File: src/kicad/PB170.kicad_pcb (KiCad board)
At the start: 4 copper layers, 61 parts, among them J2 USB_B_Micro, Q1 BC817, Q2 BC817, Q3 BC817, Q4 BC817, SW1 SW_MEC_5E, U1 74HC08, U10 74HC08, U2 74HC08, U21 74HC08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

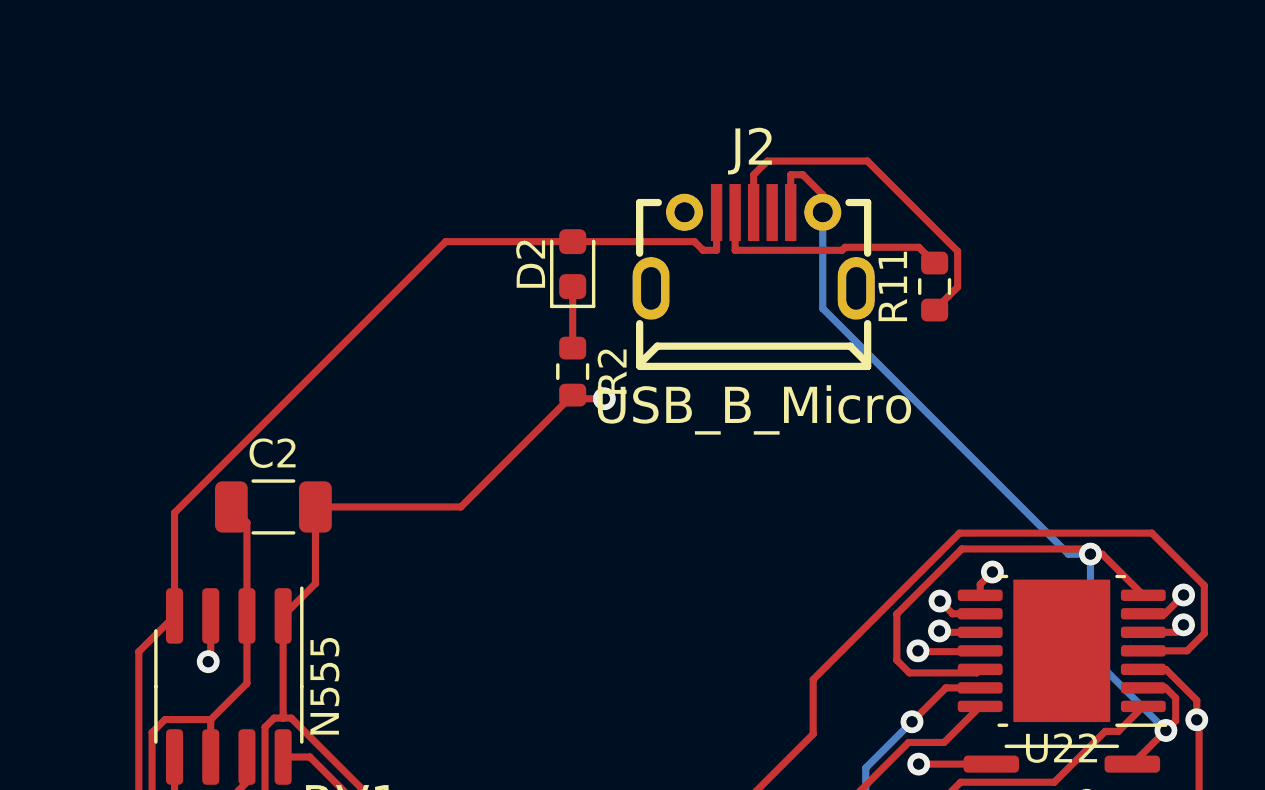
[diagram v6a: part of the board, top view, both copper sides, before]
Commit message: fixed micro-usb connection, rotated the whole thing
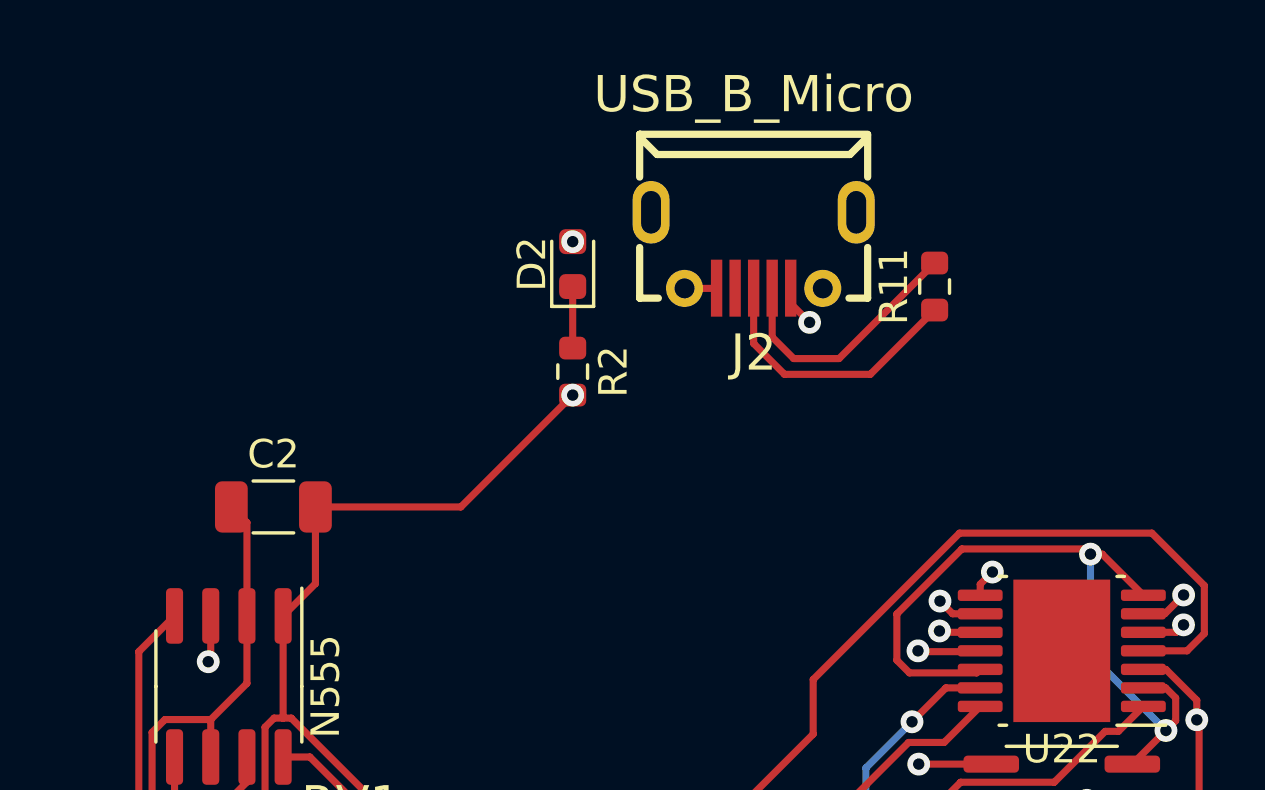
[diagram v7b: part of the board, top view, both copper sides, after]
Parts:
- turned J2 to 180 degrees
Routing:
- net /blue/VCC: track 483.4 -> 472.0 mm, vias 9 -> 11
- net GND: track 551.4 -> 544.9 mm
- net Net-(J2-Pad3): track 12.4 -> 9.68 mm
- net Net-(J2-Pad2): track 8.60 -> 9.12 mm
